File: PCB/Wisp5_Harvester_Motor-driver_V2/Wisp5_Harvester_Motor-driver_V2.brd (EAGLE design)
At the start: 30 x 30 mm, 29 parts, among them M1 PINHEAD_PINHD-1X2-1.27MM, M2 PINHEAD_PINHD-1X2-1.27MM, U1 BQ25570

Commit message: Fix the naming on the pcb and of the parts!
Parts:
- L1: value 22uH -> (none)
- L2: value 10uH -> (none)
- renumbered U$1 to WISP, U$2 to U2, U$3 to U3
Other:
- board text added: "IPR board v2.0 by Koen Schaper"
- board text added: "L1"
- board text added: "L2"
- board text added: "U2"

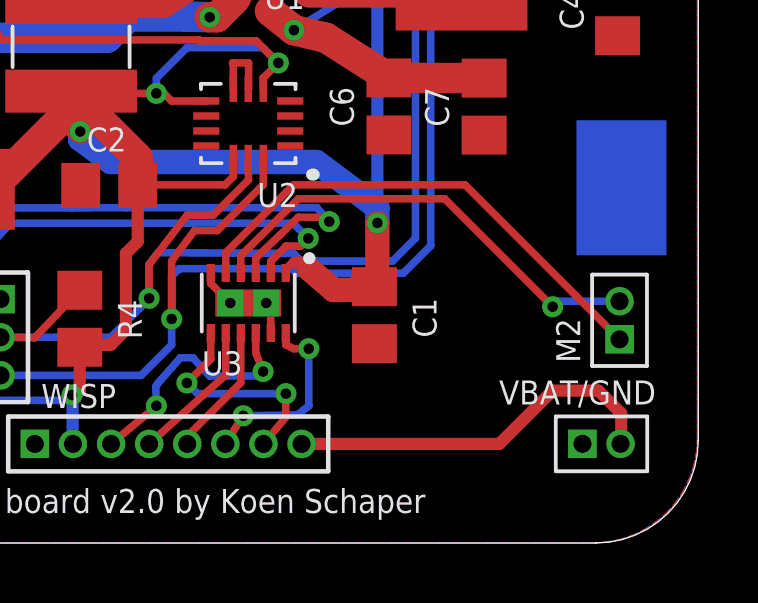
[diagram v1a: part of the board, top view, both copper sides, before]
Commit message: Add a exta bulk capacitor near the hbridge!
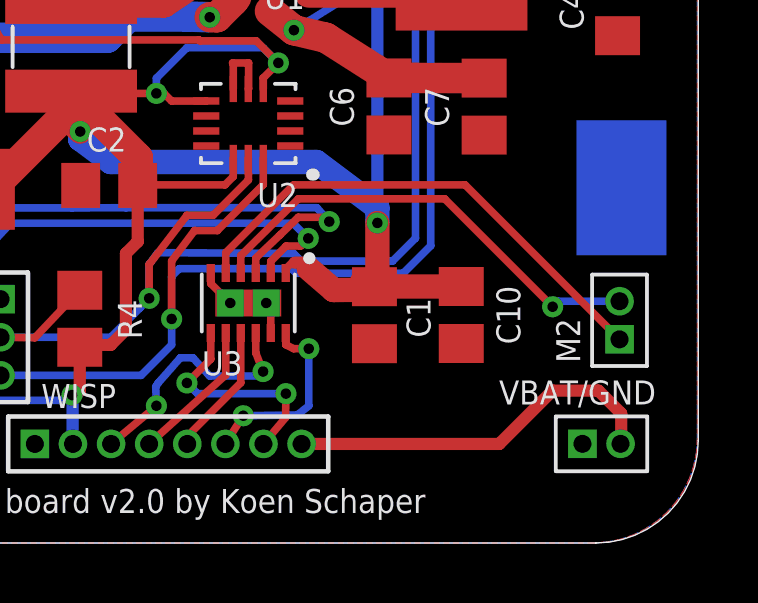
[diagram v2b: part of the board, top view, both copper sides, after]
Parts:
- added C10: DNP, rcl:C0805
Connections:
- net GND: now also C10.2
- net VREG: now also C10.1
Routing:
- net VREG: track 101.5 -> 104.3 mm
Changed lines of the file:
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@@
 <elements>
 <element name="C1" library="rcl" library_urn="urn:adsk.eagle:library:334" package="C0805" value="0.1uF" x="19.206" y="7.594" smashed="yes" rot="R270">
-<attribute name="NAME" x="20.476" y="8.164" size="0.8" layer="25" rot="R270"/>
+<attribute name="NAME" x="20.276" y="8.164" size="0.8" layer="25" rot="R270"/>
 <attribute name="VALUE" x="16.666" y="8.864" size="0.8" layer="27" rot="R270"/>
 </element>
@@
 <element name="MAX44000" library="Wisp5_Harvester_Motor-driver_V2" package="PINHEAD_1X04-1.27MM" value="PINHEAD_PINHD-1X4-1.27MM" x="13.1" y="27.1" smashed="yes">
 <attribute name="NAME" x="12.2188" y="24.9113" size="0.8" layer="25" ratio="10"/>
+</element>
+<element name="C10" library="rcl" library_urn="urn:adsk.eagle:library:334" package="C0805" value="DNP" x="22.1" y="7.6" smashed="yes" rot="R270">
+<attribute name="NAME" x="23.27" y="8.57" size="0.8" layer="25" rot="R270"/>
+<attribute name="VALUE" x="19.56" y="8.87" size="0.8" layer="27" rot="R270"/>
 </element>
 </elements>
@@
 <wire x1="13.75" y1="9" x2="13.75" y2="8.65" width="0.254" layer="1"/>
 <wire x1="13.75" y1="8.65" x2="14.4" y2="8" width="0.254" layer="1"/>
+<contactref element="C10" pad="2"/>
 </signal>
 <signal name="VREG">
@@
 <wire x1="9.144" y1="4.9138625" x2="9.125425" y2="4.9324375" width="0.4064" layer="16"/>
 <wire x1="9.144" y1="3.3147" x2="9.144" y2="4.9138625" width="0.4064" layer="16"/>
+<contactref element="C10" pad="1"/>
+<wire x1="22.1" y1="8.55" x2="19.409265625" y2="8.55" width="0.8128" layer="1"/>
+<wire x1="19.409265625" y1="8.55" x2="19.304" y2="8.444734375" width="0.8128" layer="1"/>
 </signal>
 <signal name="VBOOST">

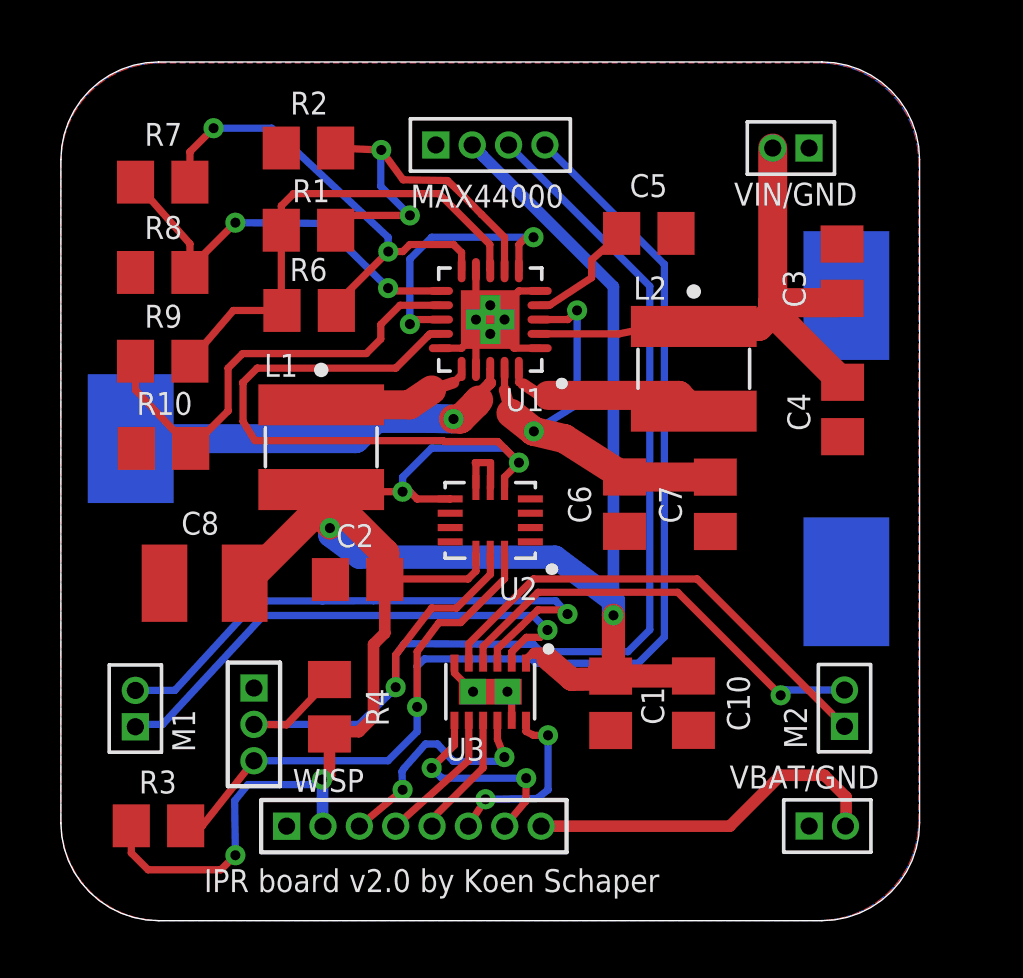
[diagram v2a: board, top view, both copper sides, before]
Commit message: Small changes to the layout and added missing inductor values!
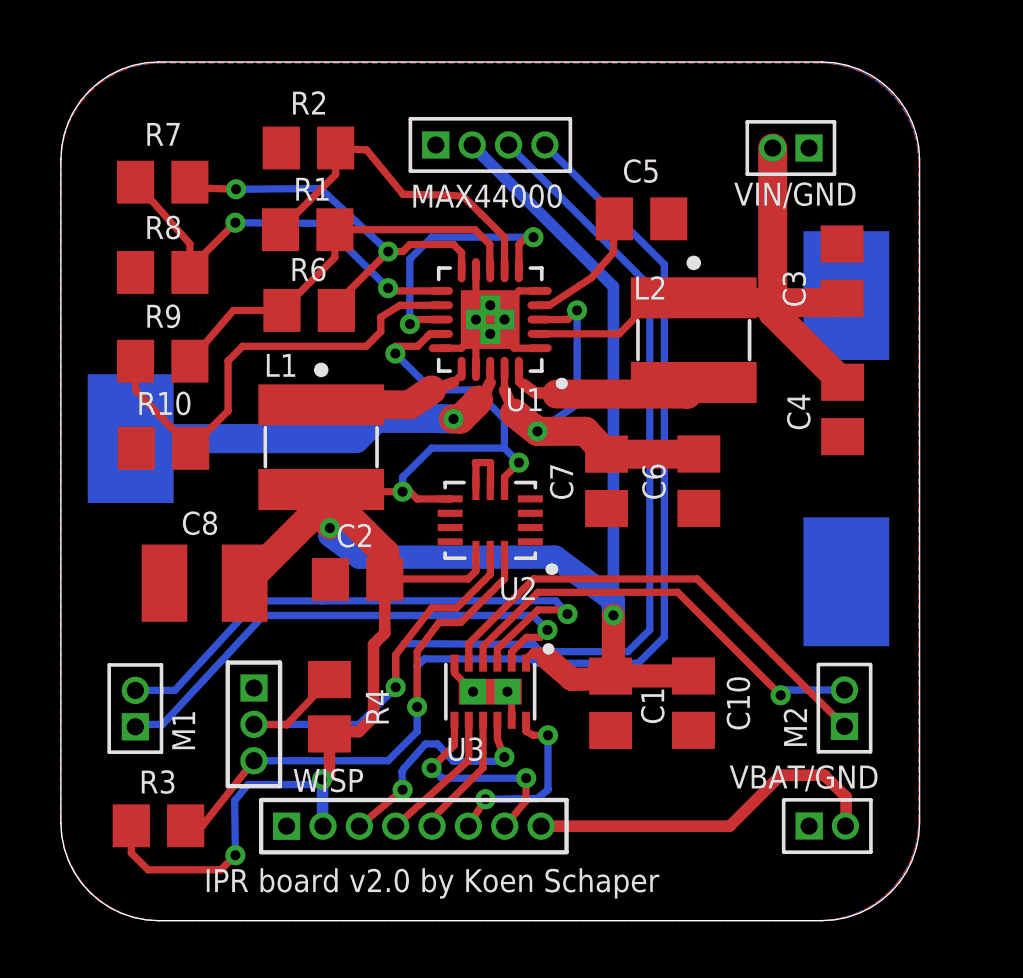
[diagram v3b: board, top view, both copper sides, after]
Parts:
- L1: value (none) -> 22uH
- L2: value (none) -> 10uH
- moved C7 3.88 mm to (19.1, 15.3)
- moved C6 2.72 mm to (22.3, 15.4)
- moved L1 1.00 mm to (22.1, 20.3)
- moved C5 0.57 mm to (20.3, 24.5)
- turned R1 to 0 degrees
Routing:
- net VREG: track 104.3 -> 92.8 mm, vias 6 -> 7
- net N$2: track 17.2 -> 14.4 mm
- net N$10: track 16.5 -> 14.0 mm
- net N$13: track 13.9 -> 12.0 mm, vias 2 -> 0
- net VBAT: track 14.0 -> 14.8 mm
- net VSTOR: track 15.9 -> 15.1 mm
- net VHARV: track 20.1 -> 20.6 mm

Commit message: Non power return paths!
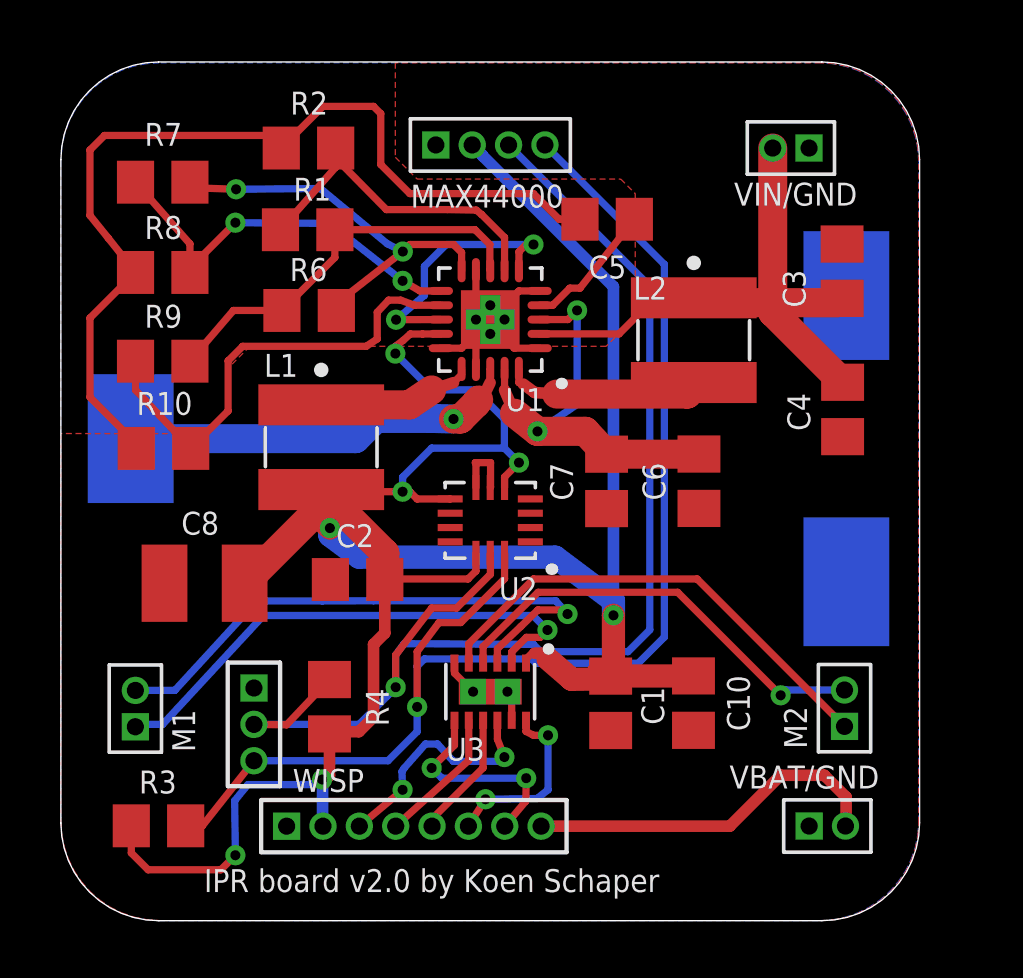
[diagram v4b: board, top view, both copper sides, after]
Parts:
- moved C5 1.20 mm to (19.1, 24.5), turned to 180 degrees
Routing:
- net GND: track 14.9 -> 48.0 mm

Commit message: Final design for proximity and harvester board
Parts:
- moved C5 0.57 mm to (19.6, 24.2)
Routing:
- net GND: track 48.0 -> 48.6 mm
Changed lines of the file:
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@@
 <attribute name="VALUE" x="24.77" y="19.13" size="0.8" layer="27" rot="R270"/>
 </element>
-<element name="C5" library="rcl" library_urn="urn:adsk.eagle:library:334" package="C0805" value="10nF" x="19.084" y="24.504" smashed="yes" rot="R180">
-<attribute name="NAME" x="19.754" y="23.234" size="0.8" layer="25" rot="R180"/>
-<attribute name="VALUE" x="20.354" y="27.044" size="0.8" layer="27" rot="R180"/>
+<element name="C5" library="rcl" library_urn="urn:adsk.eagle:library:334" package="C0805" value="10nF" x="19.592" y="24.25" smashed="yes" rot="R180">
+<attribute name="NAME" x="20.1604" y="26.282" size="0.8" layer="25" rot="R180"/>
+<attribute name="VALUE" x="20.862" y="26.79" size="0.8" layer="27" rot="R180"/>
 </element>
 <element name="C6" library="rcl" library_urn="urn:adsk.eagle:library:334" package="C0805" value="4.7uF" x="22.29" y="15.352" smashed="yes" rot="R90">
@@
 <wire x1="11.176" y1="26.416" x2="12.192" y2="25.4" width="0.254" layer="1"/>
 <wire x1="12.192" y1="25.4" x2="16.51" y2="25.4" width="0.254" layer="1"/>
-<wire x1="16.51" y1="25.4" x2="17.406" y2="24.504" width="0.254" layer="1"/>
-<wire x1="17.406" y1="24.504" x2="18.134" y2="24.504" width="0.254" layer="1"/>
+<wire x1="16.51" y1="25.4" x2="17.66" y2="24.25" width="0.254" layer="1"/>
+<wire x1="17.66" y1="24.25" x2="18.642" y2="24.25" width="0.254" layer="1"/>
 <polygon width="0.254" layer="1">
 <vertex x="11.684" y="29.972"/>
@@
 <wire x1="16.725" y1="21.5" x2="17.182" y2="21.5" width="0.254" layer="1"/>
 <wire x1="17.182" y1="21.5" x2="17.78" y2="22.098" width="0.254" layer="1"/>
-<wire x1="18.136" y1="22.098" x2="20.034" y2="24.504" width="0.254" layer="1"/>
-<wire x1="17.78" y1="22.098" x2="18.136" y2="22.098" width="0.254" layer="1"/>
+<wire x1="18.644" y1="22.098" x2="20.542" y2="24.25" width="0.254" layer="1"/>
+<wire x1="17.78" y1="22.098" x2="18.644" y2="22.098" width="0.254" layer="1"/>
 </signal>
 <signal name="N$4">
